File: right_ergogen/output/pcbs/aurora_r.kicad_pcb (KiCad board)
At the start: 2 copper layers, 161.2 x 132.9 mm, 124 parts

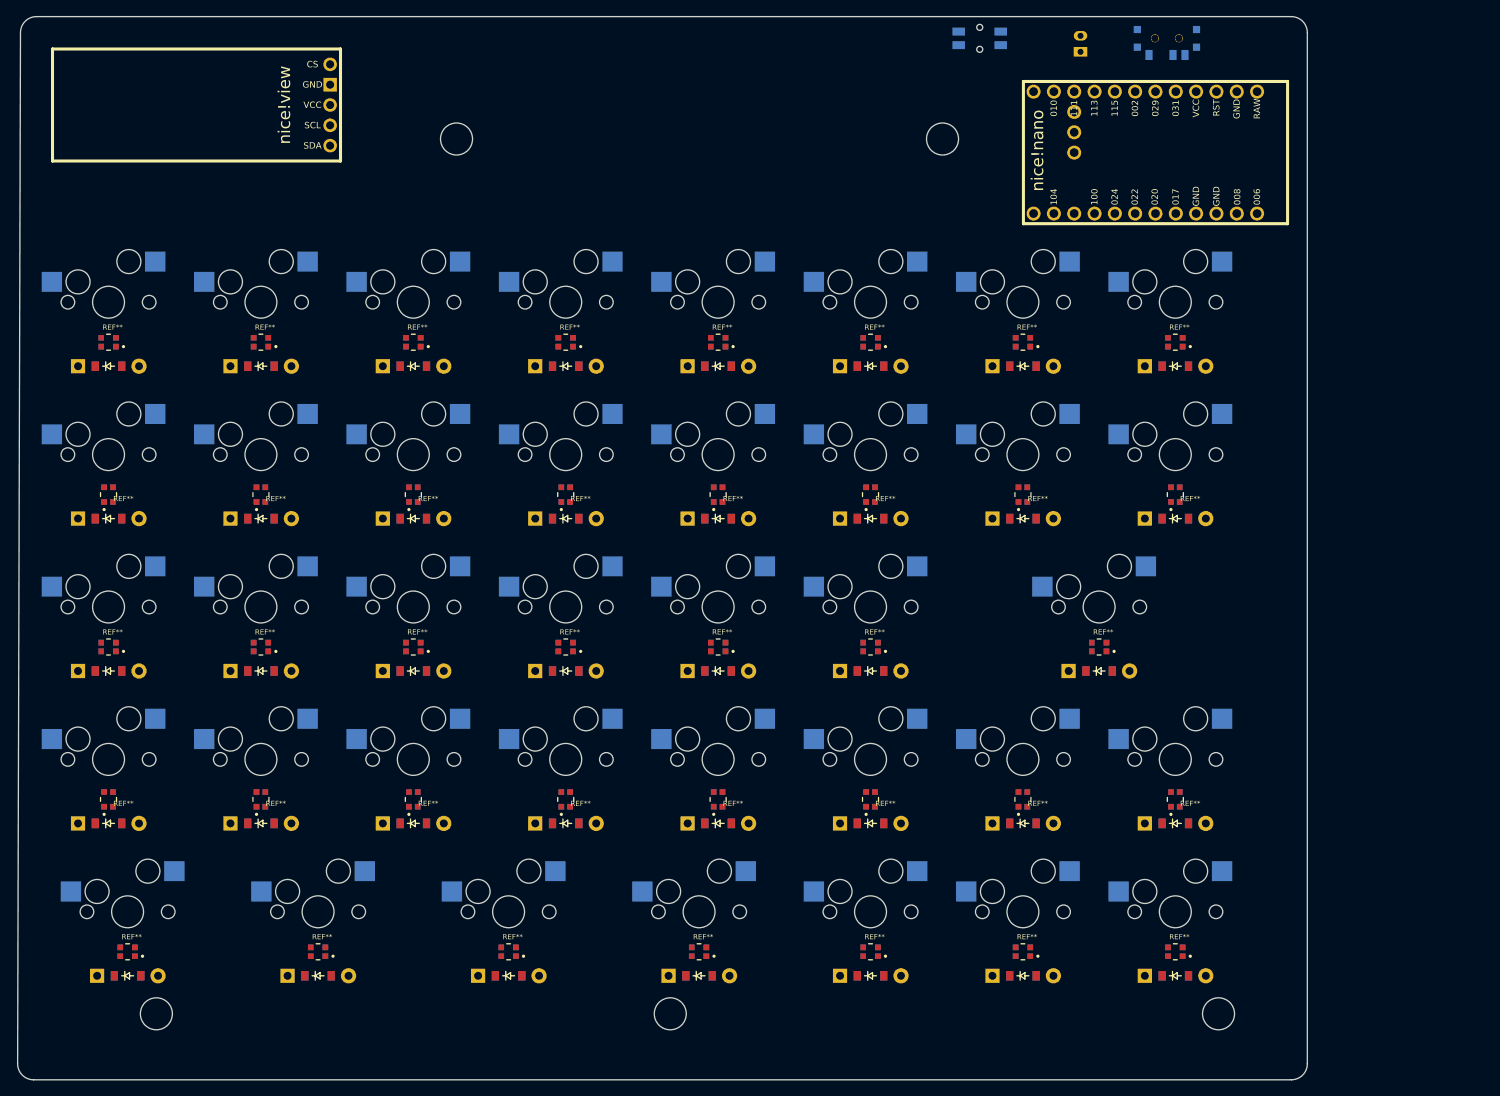
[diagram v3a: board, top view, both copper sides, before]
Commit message: Full redesign of right side with rotary encoder
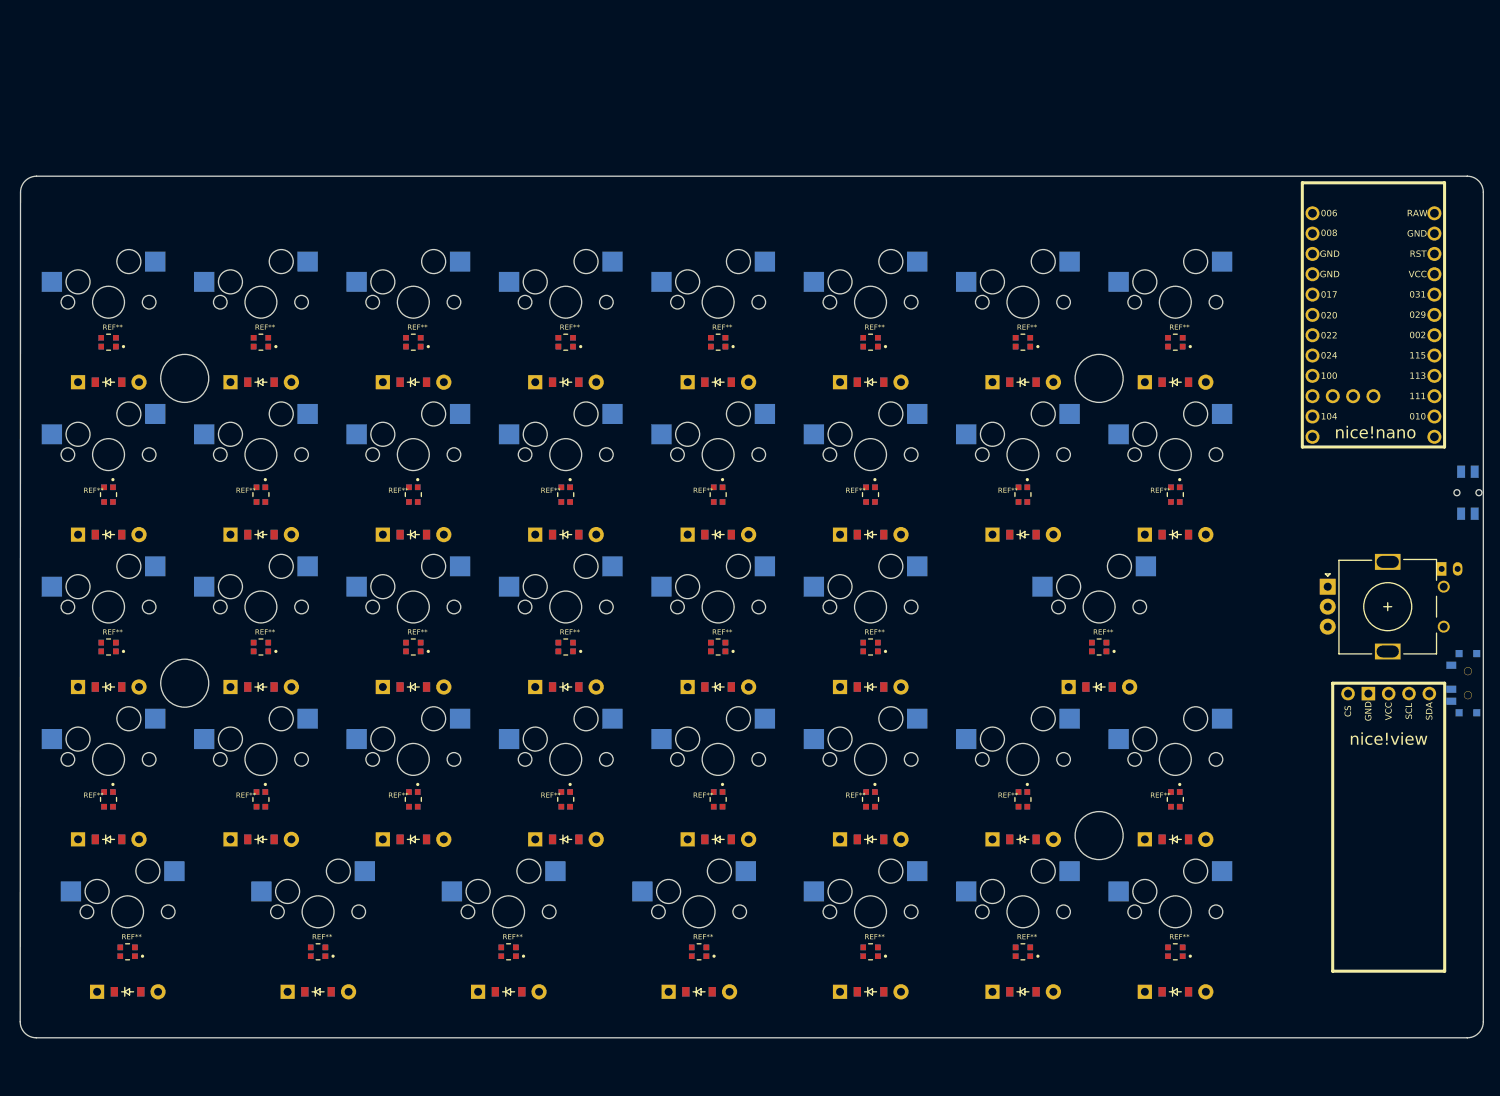
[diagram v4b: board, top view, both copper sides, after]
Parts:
- removed the ? at (143.5, 60.6)
- removed the ? at (204.2, 60.6)
- removed the ? at (170.2, 169.9)
- removed the ? at (106.0, 169.9)
- removed the ? at (238.8, 169.9)
- added ?: , HOLE_M2_TH, F.Cu at (109.5, 90.5)
- added ?: , HOLE_M2_TH, F.Cu at (223.8, 90.5)
- added ?: , HOLE_M2_TH, F.Cu at (109.5, 128.6)
- added ?: , HOLE_M2_TH, F.Cu at (223.8, 147.6)
- added ROT1: , rotary_encoder, F.Cu at (260.0, 119.0)
- moved niceView1 149.6 mm to (260.0, 128.6), turned to -90 degrees
- moved T1 89.0 mm to (269.9, 128.6), turned to 270 degrees
- moved B1 83.4 mm to (269.9, 104.8), turned to 270 degrees
- moved JST1 80.2 mm to (267.6, 114.3), turned to 0 degrees
- moved MCU1 35.7 mm to (258.1, 83.8), turned to -90 degrees
- moved D17 2.00 mm to (100.0, 129.1)
- moved D18 2.00 mm to (119.0, 129.1)
- moved D19 2.00 mm to (138.1, 129.1)
- moved D20 2.00 mm to (157.2, 129.1)
- moved D21 2.00 mm to (176.2, 129.1)
- moved D22 2.00 mm to (195.2, 129.1)
- moved D23 2.00 mm to (223.8, 129.1)
- moved D1 2.00 mm to (100.0, 110.0)
- moved D10 2.00 mm to (176.2, 91.0)
- moved D11 2.00 mm to (195.2, 110.0)
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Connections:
- D1 pad 1: P002 -> P029
- D10 pad 1: P029 -> P031
- D11 pad 1: P002 -> P029
- D12 pad 1: P029 -> P031
- D13 pad 1: P002 -> P029
- D14 pad 1: P029 -> P031
- D15 pad 1: P002 -> P029
- D16 pad 1: P029 -> P031
- D17 pad 1: P115 -> P002
- D18 pad 1: P115 -> P002
- D19 pad 1: P115 -> P002
- D2 pad 1: P029 -> P031
- D20 pad 1: P115 -> P002
- D21 pad 1: P115 -> P002
- D22 pad 1: P115 -> P002
- D23 pad 1: P115 -> P002
- D24 pad 1: P113 -> P115
- D25 pad 1: P113 -> P115
- D26 pad 1: P113 -> P115
- D27 pad 1: P113 -> P115
- D28 pad 1: P113 -> P115
- D29 pad 1: P113 -> P115
- D3 pad 1: P002 -> P029
- D30 pad 1: P113 -> P115
- D31 pad 1: P113 -> P115
- D32 pad 1: P031 -> P113
- D33 pad 1: P031 -> P113
- D34 pad 1: P031 -> P113
- D35 pad 1: P031 -> P113
- D36 pad 1: P031 -> P113
- D37 pad 1: P031 -> P113
- D38 pad 1: P031 -> P113
- D4 pad 1: P029 -> P031
- D5 pad 1: P002 -> P029
- D6 pad 1: P029 -> P031
- D7 pad 1: P002 -> P029
- D8 pad 1: P029 -> P031
- D9 pad 1: P002 -> P029
- REF** pad 2: P8 -> P010 (x38)
- REF** pad 4: P15 -> P009 (x38)
- S1 pad 2: P020 -> P106
- S10 pad 2: P011 -> P024
- S11 pad 2: P017 -> P022
- S12 pad 2: P017 -> P022
- S13 pad 2: P104 -> P020
- S14 pad 2: P104 -> P020
- S15 pad 2: P106 -> P017
- S16 pad 2: P106 -> P017
- S17 pad 2: P020 -> P106
- S18 pad 2: P022 -> P104
- S19 pad 2: P024 -> P011
- S2 pad 2: P020 -> P106
- S21 pad 2: P011 -> P024
- S22 pad 2: P017 -> P022
- S23 pad 2: P104 -> P020
- S24 pad 2: P020 -> P106
- S25 pad 2: P022 -> P104
- S26 pad 2: P024 -> P011
- S28 pad 2: P011 -> P024
- S29 pad 2: P017 -> P022
- S3 pad 2: P022 -> P104
- S30 pad 2: P104 -> P020
- S31 pad 2: P106 -> P017
- S32 pad 2: P020 -> P106
- S33 pad 2: P022 -> P104
- S34 pad 2: P100 -> P011
- S35 pad 2: P011 -> P100
- S36 pad 2: P017 -> P022
- S37 pad 2: P104 -> P020
- S38 pad 2: P106 -> P017
- S4 pad 2: P022 -> P104
- S5 pad 2: P024 -> P011
- S6 pad 2: P024 -> P011
- S9 pad 2: P011 -> P024
- niceView1 pad 1: P006 -> P101
- niceView1 pad 4: P020 -> P102
- niceView1 pad 5: P017 -> P107
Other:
- board size 161.2 x 132.9 mm -> 182.9 x 107.7 mm

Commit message: Rotary encoder pinout fixes
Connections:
- ROT1 pad 1: (no net) -> P111
- ROT1 pad 2: (no net) -> GND
- ROT1 pad B: GND -> P008
- ROT1 pad C: P008 -> GND
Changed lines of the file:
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@@
             (fp_circle (center -0.12 -0.04) (end 2.88 -0.04) (layer F.Fab) (width 0.12))
             (pad A thru_hole rect (at -7.62 -2.54 0) (size 2 2) (drill 1) (layers *.Cu *.Mask) (net 59 "P006"))
-            (pad C thru_hole circle (at -7.62 -0.04) (size 2 2) (drill 1) (layers *.Cu *.Mask) (net 60 "P008"))
-            (pad B thru_hole circle (at -7.62 2.46) (size 2 2) (drill 1) (layers *.Cu *.Mask) (net 55 "GND"))
-            (pad 1 thru_hole circle (at 6.88 -2.54) (size 1.5 1.5) (drill 1) (layers *.Cu *.Mask) (net 0 ""))
-            (pad 2 thru_hole circle (at 6.88 2.46) (size 1.5 1.5) (drill 1) (layers *.Cu *.Mask) (net 0 ""))
+            (pad C thru_hole circle (at -7.62 -0.04) (size 2 2) (drill 1) (layers *.Cu *.Mask) (net 55 "GND"))
+            (pad B thru_hole circle (at -7.62 2.46) (size 2 2) (drill 1) (layers *.Cu *.Mask) (net 60 "P008"))
+            (pad 1 thru_hole circle (at 6.88 -2.54) (size 1.5 1.5) (drill 1) (layers *.Cu *.Mask) (net 58 "P111"))
+            (pad 2 thru_hole circle (at 6.88 2.46) (size 1.5 1.5) (drill 1) (layers *.Cu *.Mask) (net 55 "GND"))
             (pad "" thru_hole rect (at -0.12 -5.64 0) (size 3.2 2) (drill oval 2.8 1.5) (layers *.Cu *.Mask))
             (pad "" thru_hole rect (at -0.12 5.56 0)  (size 3.2 2) (drill oval 2.8 1.5) (layers *.Cu *.Mask))
